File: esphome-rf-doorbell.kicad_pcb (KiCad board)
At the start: 2 copper layers, 65 x 54.7 mm, 58 parts, among them J1 B4B-XH, J2 CONUFL001-SMD-T, J3 PROG, SW1 Boot, U1 ESP32-S2-MINI-2, U2 RFM95W-868S2, U3 TLP2391, U4 G3VM-63ER, U5 MP5493GJ-Z, U6 ASSR-1218

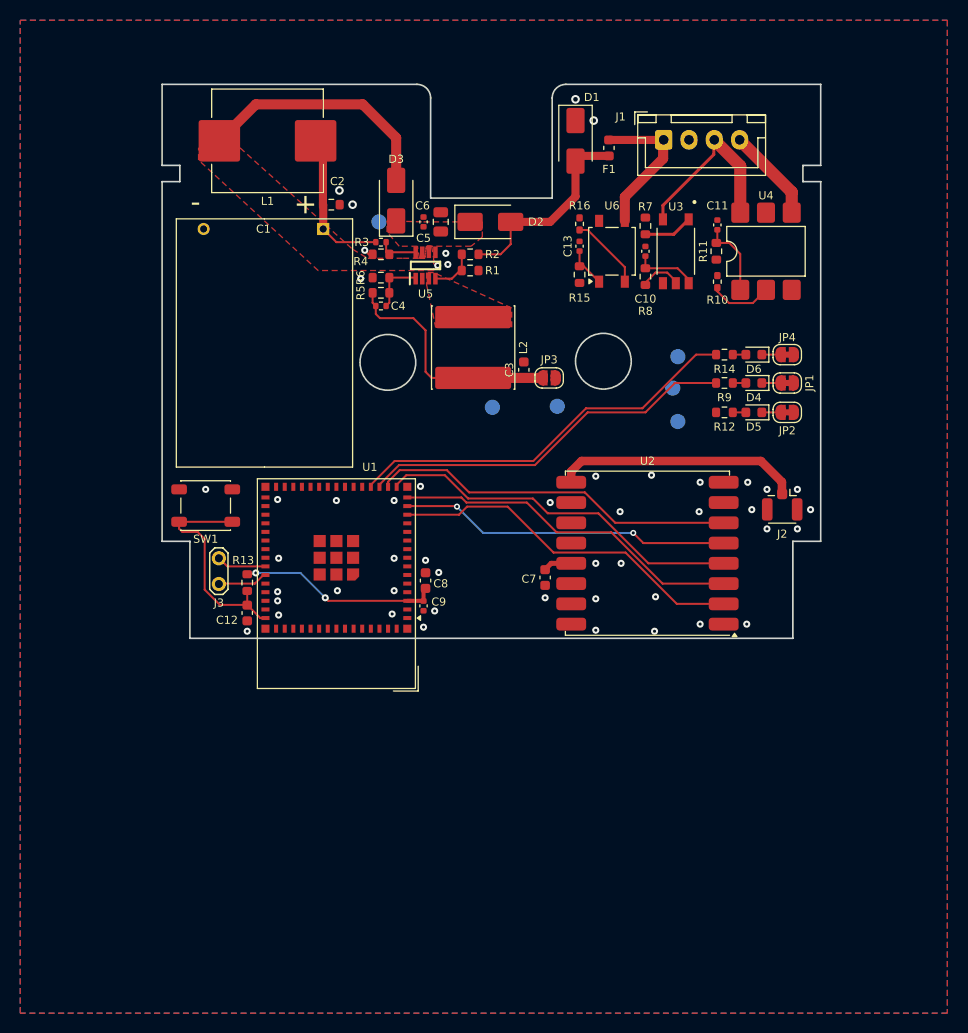
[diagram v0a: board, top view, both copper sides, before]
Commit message: Replace RF module, finish routing
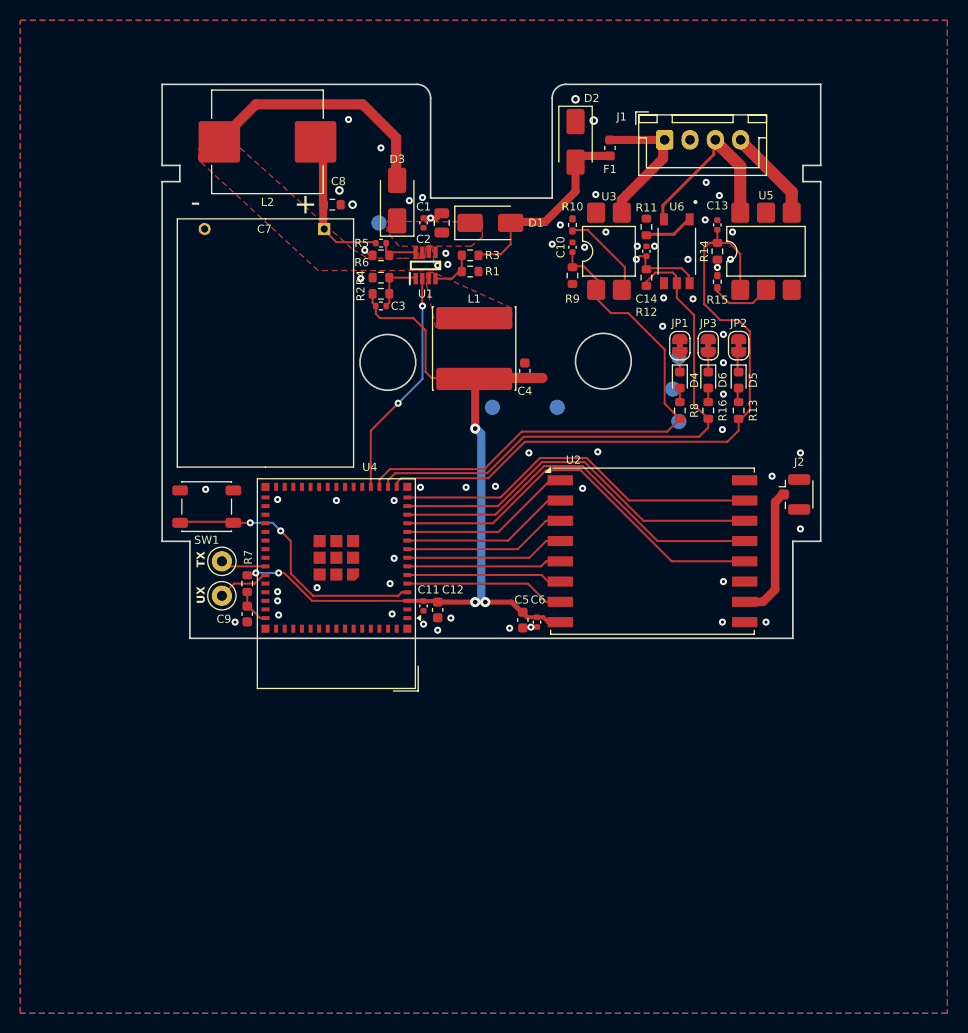
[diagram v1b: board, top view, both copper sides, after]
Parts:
- removed the JP3 at (146.2, 95.3)
- added C6: 0.1uF, Capacitor_SMD:C_0402_1005Metric, F.Cu at (145.0, 119.4)
- added J4: Conn_01x01, TestPoint:TestPoint_Keystone_5000-5004_Miniature, F.Cu at (113.9, 116.8)
- J3: value PROG -> Conn_01x01; footprint TestPoint:TestPoint_2Pads_Pitch2.54mm_Drill0.8mm -> TestPoint:TestPoint_Keystone_5000-5004_Miniature
- U2: value RFM95W-868S2 -> RFM69W; footprint RF_Module:HOPERF_RFM9XW_SMD -> RF_Module:HOPERF_RFM69HW
- U3: renamed from U6; value ASSR-1218 -> G3VM-31DR; footprint Package_SO:SO-4_4.4x4.3mm_P2.54mm -> Package_DIP:SMDIP-4_W7.62mm
- moved JP1 10.6 mm to (159.1, 92.1), turned to -90 degrees
- moved JP3 8.63 mm to (161.9, 92.1), turned to -90 degrees
- moved JP2 8.15 mm to (164.9, 92.1), turned to -90 degrees
- moved D4 7.72 mm to (159.1, 95.5), turned to -90 degrees
- moved R8 7.05 mm to (159.1, 98.5), turned to -90 degrees
- moved C5 4.74 mm to (143.6, 119.2)
- moved D6 4.51 mm to (161.9, 95.5), turned to -90 degrees
- moved D5 3.52 mm to (164.9, 95.5), turned to -90 degrees
- moved R16 3.15 mm to (161.9, 98.5), turned to -90 degrees
- moved C11 3.14 mm to (135.2, 118.2), turned to -90 degrees
- moved J2 1.56 mm to (170.4, 106.8), turned to 0 degrees
- moved R13 1.41 mm to (164.9, 98.5), turned to -90 degrees
- moved C10 0.71 mm to (148.5, 82.4)
- moved R10 0.71 mm to (148.5, 80.2)
- moved R9 0.71 mm to (148.5, 85.2)
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- renumbered C6 to C1, C13 to C10, C8 to C11, C9 to C12, C11 to C13, C10 to C14, C5 to C2, C4 to C3, C3 to C4, C7 to C5, C1 to C7, C2 to C8, C12 to C9, D2 to D1, D1 to D2, D6 to D4, D4 to D6, JP4 to JP1, JP1 to JP3, L2 to L1, L1 to L2, R16 to R10, R7 to R11, R8 to R12, R12 to R13, R11 to R14, R10 to R15, R9 to R16, R5 to R2, R2 to R3, R6 to R4, R3 to R5, R4 to R6, R13 to R7, R14 to R8, R15 to R9, U5 to U1, U1 to U4, U4 to U5, U3 to U6
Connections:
- C3 pad 1: Net-(JP3-A) -> +3.3V
- C4 pad 1: Net-(JP3-A) -> +3.3V
- C9 pad 1: /EN -> Net-(U4-EN)
- L1 pad 2: Net-(JP3-A) -> +3.3V
- R2 pad 1: Net-(JP3-A) -> +3.3V
- R7 pad 2: /EN -> Net-(U4-EN)
- SW1 pad 2: /EN -> Net-(U4-IO0)
- U1 pad 2: unconnected-(U5-PFAIL-Pad2) -> /~{POWER_FAIL}
- U2 pad 1: GND -> /RF.Reset
- U2 pad 10: GND -> /RF.Antenna
- U2 pad 11: unconnected-(U2-DIO3-Pad11) -> GND
- U2 pad 12: unconnected-(U2-DIO4-Pad12) -> /RF.SCLK
- U2 pad 13: +3.3V -> /RF.MISO
- U2 pad 14: unconnected-(U2-DIO0-Pad14) -> /RF.MOSI
- U2 pad 15: unconnected-(U2-DIO1-Pad15) -> /RF.CE
- U2 pad 2: /RF.MISO -> /RF.IO0
- U2 pad 3: /RF.MOSI -> /RF.IO1
- U2 pad 4: /RF.SCLK -> /RF.IO2
- U2 pad 5: /RF.CE -> /RF.IO3
- U2 pad 6: /RF.Reset -> /RF.IO4
- U2 pad 7: unconnected-(U2-DIO5-Pad7) -> /RF.IO5
- U2 pad 8: GND -> +3.3V
- U2 pad 9: /RF.Antenna -> GND
- U4 pad 10: unconnected-(U1-IO6-Pad10) -> /RF.IO0
- U4 pad 11: unconnected-(U1-IO7-Pad11) -> /RF.Reset
- U4 pad 12: unconnected-(U1-IO8-Pad12) -> /RF.SCLK
- U4 pad 14: /RF.CE -> /RF.MOSI
- U4 pad 15: /RF.MOSI -> /RF.CE
- U4 pad 16: /RF.SCLK -> /BELL_OFF
- U4 pad 17: /RF.Reset -> /~{BELL_SIGNAL}
- U4 pad 18: /~{BELL_SIGNAL} -> /OPEN_BUZZER
- U4 pad 19: /OPEN_BUZZER -> /~{POWER_FAIL}
- U4 pad 20: /BELL_OFF -> unconnected-(U4-IO16-Pad20)
- U4 pad 4: unconnected-(U1-IO0-Pad4) -> Net-(U4-IO0)
- U4 pad 45: /EN -> Net-(U4-EN)
- U4 pad 5: unconnected-(U1-IO1-Pad5) -> /RF.IO5
- U4 pad 6: unconnected-(U1-IO2-Pad6) -> /RF.IO4
- U4 pad 7: unconnected-(U1-IO3-Pad7) -> /RF.IO3
- U4 pad 8: unconnected-(U1-IO4-Pad8) -> /RF.IO2
- U4 pad 9: unconnected-(U1-IO5-Pad9) -> /RF.IO1
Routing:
- net /BELL_OFF: track 7.70 -> 67.0 mm
- net +3.3V: track 29.1 -> 87.6 mm, vias 2 -> 6
- net Net-(U4-IO0): track 0.00 -> 27.6 mm, vias 0 -> 2
- net Net-(JP3-A): track 23.7 -> 0.00 mm
- net /~{POWER_FAIL}: track 0.00 -> 22.7 mm, vias 0 -> 2
- net /EN: track 22.4 -> 0.00 mm
- net /RF.Reset: track 36.3 -> 17.1 mm
- net /RF.IO0: track 0.00 -> 16.6 mm
- net /RF.IO1: track 0.00 -> 16.2 mm
- net /RF.IO5: track 0.00 -> 15.7 mm
- net /RF.IO2: track 0.00 -> 15.7 mm
- net /RF.IO4: track 0.00 -> 15.3 mm
- net /RF.IO3: track 0.00 -> 15.2 mm
- net /~{BELL_SIGNAL}: track 41.8 -> 54.5 mm
- net /RF.Antenna: track 24.4 -> 13.3 mm
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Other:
- board text added: "TX"
- board text added: "UX"
